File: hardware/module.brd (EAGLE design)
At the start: 109.9 x 68.6 mm, 118 parts, among them IC1 IC_USBLC6-2, IC2 LM1117IMPX-3.3, IC3 PIC32MX795F512, IC4 DP83848, IC5 LM1117MPX-2.5, U1 USD-SOCKETUSD, U2 VS1003, X2 CRYSTALS-NOGND-CFPX-217, X3 KUSBVX, Y3 CRYSTAL-GROUNDEDSMD-5X3.2

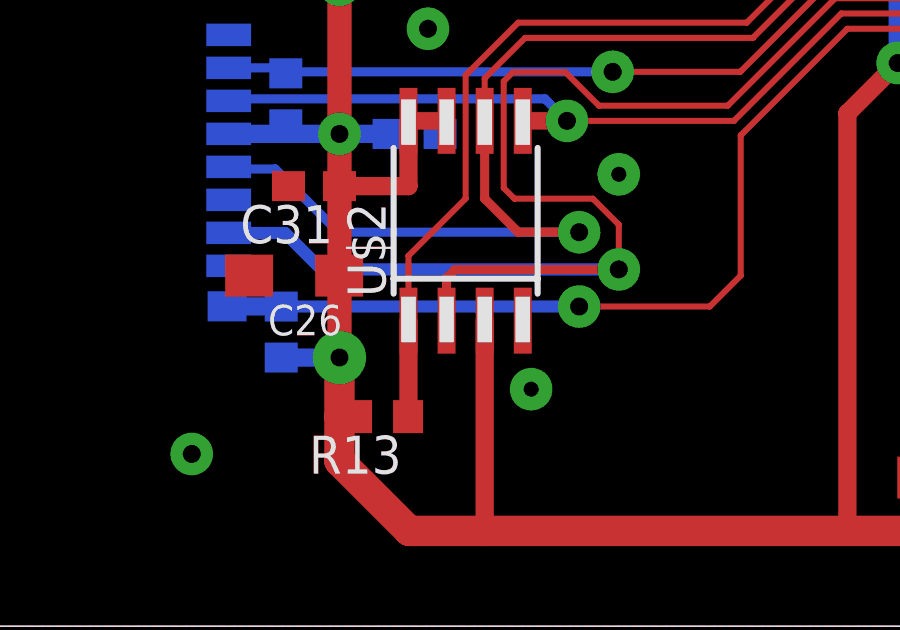
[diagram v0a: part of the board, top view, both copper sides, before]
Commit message: MISO pull-up added
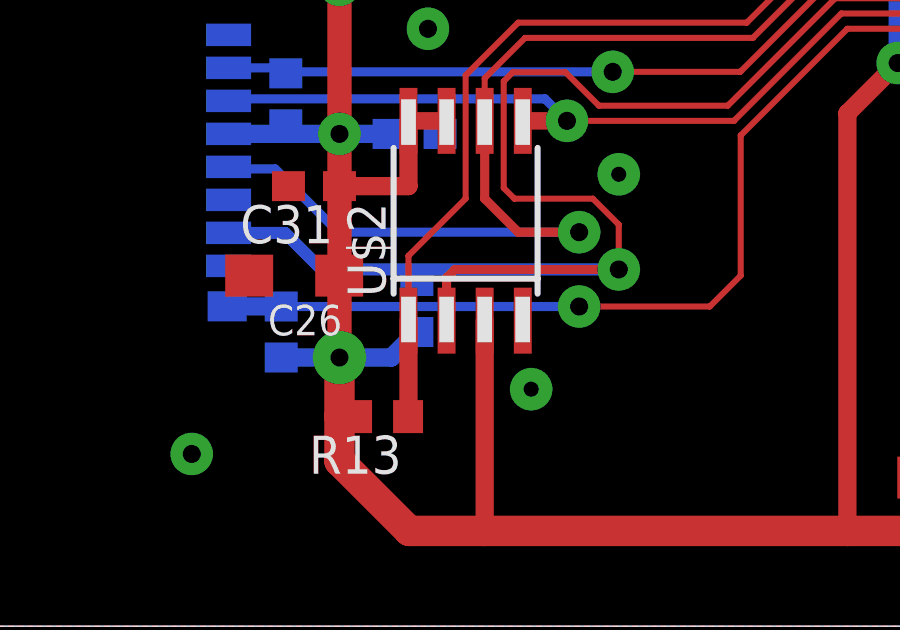
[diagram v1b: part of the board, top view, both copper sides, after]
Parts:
- added R16: (no value), rcl:R0603
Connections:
- net 3V: now also R16.2
- net MISO: now also R16.1
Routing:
- net 3V: track 523.5 -> 526.5 mm
- net MISO: track 63.6 -> 64.2 mm
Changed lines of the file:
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@@
 <element name="C2" library="rcl" package="C0402" value="" x="26.126440625" y="25.5016"/>
 <element name="L3" library="dp_devices" package="FB805" value="" x="11.938" y="38.4302" rot="MR180"/>
+<element name="R16" library="rcl" package="R0603" value="" x="20.574" y="10.6544" rot="MR270"/>
 </elements>
 <signals>
@@
 <wire x1="17.995" y1="11.43" x2="17.9846" y2="11.43" width="0.4064" layer="1"/>
 <wire x1="17.9846" y1="11.43" x2="17.9846" y2="11.684" width="0.4064" layer="1"/>
+<contactref element="R16" pad="2"/>
+<wire x1="17.995" y1="8.9544" x2="19.724" y2="8.9544" width="0.6096" layer="16"/>
+<wire x1="19.724" y1="8.9544" x2="20.574" y2="9.8044" width="0.6096" layer="16"/>
 </signal>
 <signal name="SOSCI">
@@
 <wire x1="14.3036" y1="13.1064" x2="14.3" y2="13.11" width="0.4064" layer="16"/>
 <wire x1="34.5186" y1="20.9296" x2="37.719" y2="20.9296" width="0.2032" layer="1"/>
-<wire x1="27.305" y1="11.8908" x2="17.3954" y2="11.8908" width="0.4064" layer="16"/>
+<wire x1="27.305" y1="11.8908" x2="20.32" y2="11.8908" width="0.4064" layer="16"/>
+<wire x1="20.32" y1="11.8908" x2="17.3954" y2="11.8908" width="0.4064" layer="16"/>
 <wire x1="27.305" y1="11.8908" x2="21.8476" y2="11.8908" width="0.3048" layer="1"/>
 <wire x1="21.8476" y1="11.8908" x2="21.5646" y2="11.6078" width="0.3048" layer="1"/>
@@
 <wire x1="23.7744" y1="18.4658" x2="25.527" y2="18.4658" width="0.2032" layer="1"/>
 <wire x1="26.6446" y1="17.3482" x2="30.9372" y2="17.3482" width="0.2032" layer="1"/>
+<contactref element="R16" pad="1"/>
+<wire x1="20.574" y1="11.5044" x2="20.32" y2="11.5044" width="0.3048" layer="16"/>
+<wire x1="20.32" y1="11.5044" x2="20.32" y2="11.8908" width="0.3048" layer="16"/>
 </signal>
 <signal name="MOSI">
@@
 <via x="25.9842" y="10.6544" extent="1-16" drill="0.6" diameter="1.4224" shape="octagon"/>
 <wire x1="16.0528" y1="10.6544" x2="16.09" y2="10.6544" width="0.3048" layer="16"/>
-<wire x1="25.9842" y1="10.6544" x2="16.0528" y2="10.6544" width="0.4064" layer="16"/>
+<wire x1="25.9842" y1="10.6544" x2="16.0528" y2="10.6544" width="0.3048" layer="16"/>
 <contactref element="IC3" pad="51"/>
 <wire x1="38.1254" y1="19.9136" x2="34.925" y2="19.9136" width="0.2032" layer="1"/>

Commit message: Fixes
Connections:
- removed net LED: SV1.6
- net RA15_ROT_SW: now also SV1.6
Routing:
- net RA15_ROT_SW: track 0.00 -> 31.6 mm
- net LED: track 23.7 -> 0.00 mm
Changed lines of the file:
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@@
 <wire x1="63.373" y1="14.351" x2="65.659" y2="12.065" width="0.2032" layer="1"/>
-</signal>
-<signal name="LED">
-<wire x1="51.892" y1="24.7906" x2="56.3372" y2="20.3454" width="0.2032" layer="1"/>
-<contactref element="SV1" pad="6"/>
-<wire x1="56.3372" y1="20.3454" x2="61.0362" y2="20.3454" width="0.2032" layer="1"/>
-<wire x1="61.0362" y1="20.3454" x2="62.865" y2="18.5166" width="0.2032" layer="1"/>
-<wire x1="62.865" y1="18.5166" x2="62.865" y2="14.1224" width="0.2032" layer="1"/>
-<wire x1="62.865" y1="14.1224" x2="64.389" y2="12.5984" width="0.2032" layer="1"/>
-<wire x1="64.389" y1="12.5984" x2="64.389" y2="10.795" width="0.2032" layer="1"/>
-<wire x1="64.389" y1="10.795" x2="65.659" y2="9.525" width="0.2032" layer="1"/>
 </signal>
 <signal name="1WIRE">
@@
 <signal name="RA15_ROT_SW">
 <contactref element="IC3" pad="67"/>
+<wire x1="51.892" y1="24.7906" x2="56.3372" y2="20.3454" width="0.2032" layer="1"/>
+<contactref element="SV1" pad="6"/>
+<wire x1="56.3372" y1="20.3454" x2="61.0362" y2="20.3454" width="0.2032" layer="1"/>
+<wire x1="61.0362" y1="20.3454" x2="62.865" y2="18.5166" width="0.2032" layer="1"/>
+<wire x1="62.865" y1="18.5166" x2="62.865" y2="14.1224" width="0.2032" layer="1"/>
+<wire x1="62.865" y1="14.1224" x2="64.389" y2="12.5984" width="0.2032" layer="1"/>
+<wire x1="64.389" y1="12.5984" x2="64.389" y2="10.795" width="0.2032" layer="1"/>
+<wire x1="64.389" y1="10.795" x2="65.659" y2="9.525" width="0.2032" layer="1"/>
+<wire x1="51.892" y1="32.6938" x2="51.892" y2="24.7906" width="0.2032" layer="1"/>
 </signal>
 </signals>
